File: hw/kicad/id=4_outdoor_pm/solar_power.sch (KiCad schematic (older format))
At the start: 5 parts

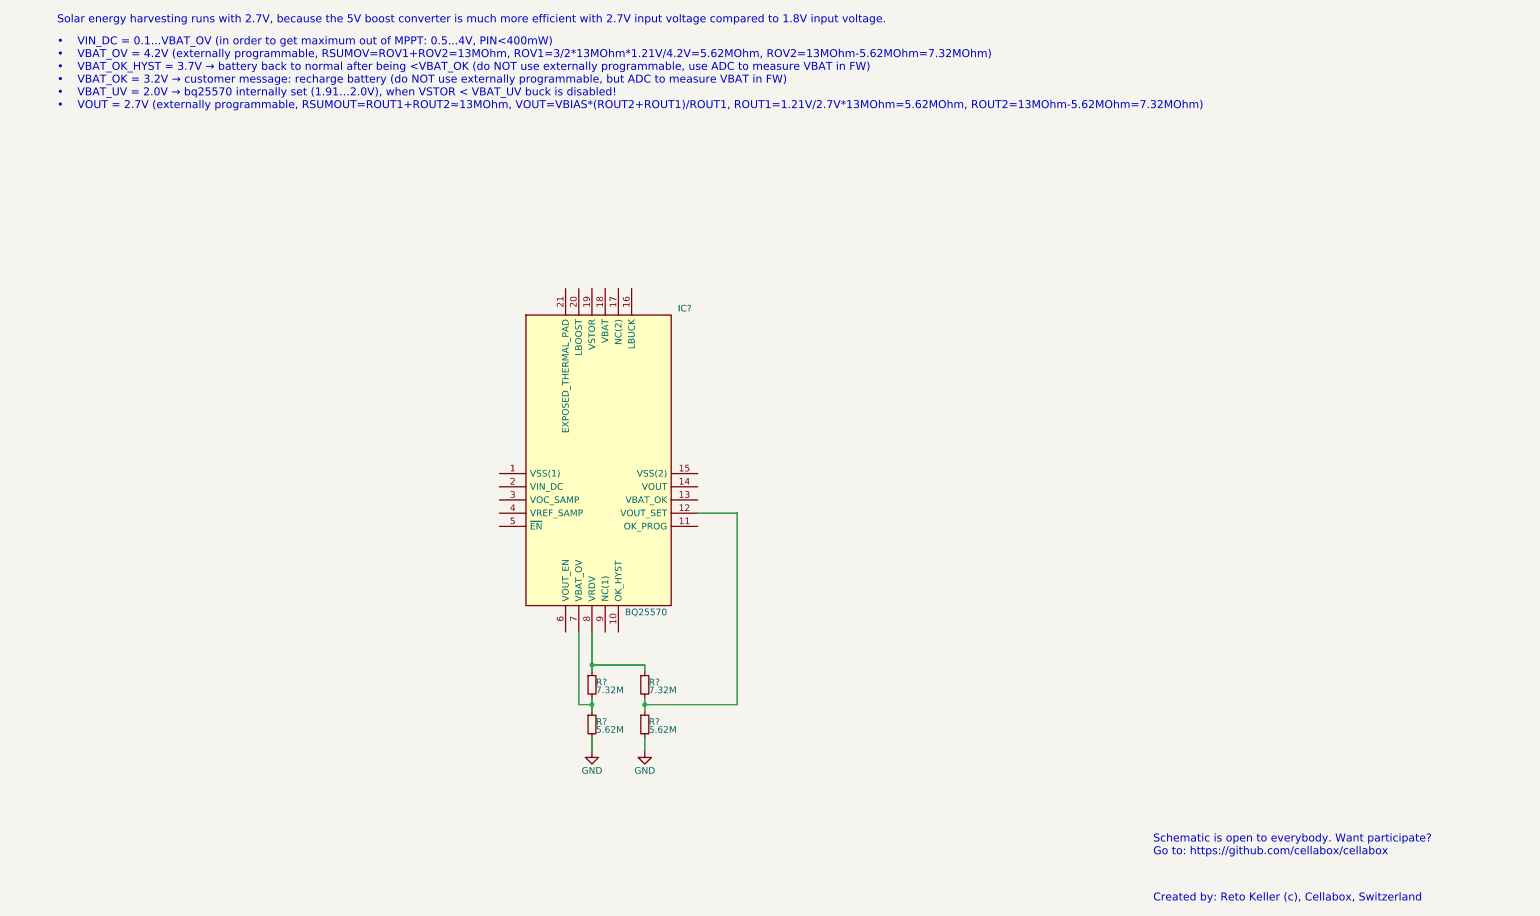
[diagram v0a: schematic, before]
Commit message: Datasheets added Schematic for outdoor PM extended
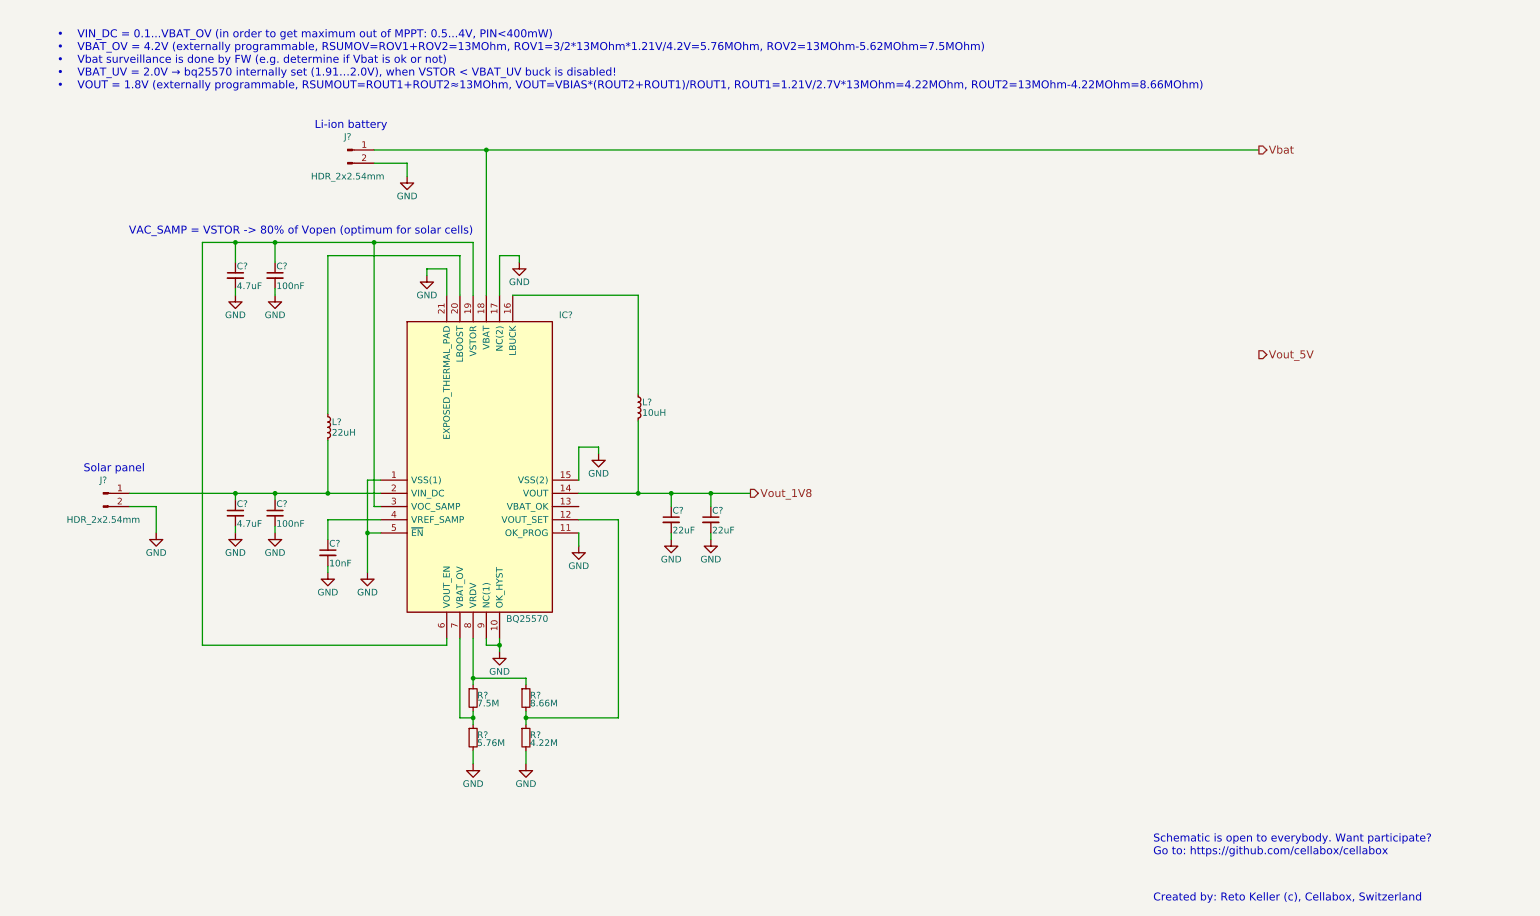
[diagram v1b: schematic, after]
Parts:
- added C? (x2): 22uF, symbol C_Small
- added C? (x2): 4.7uF, symbol C_Small
- added C? (x2): 100nF, symbol C_Small
- added C?: 10nF, symbol C_Small
- added J? (x2): HDR_2x2.54mm, symbol Conn_01x02_Male
- added L?: 10uH, symbol L_Small
- added L?: 22uH, symbol L_Small
- R?: value 7.32M -> 7.5M
- R?: value 5.62M -> 5.76M
- R?: value 5.62M -> 4.22M
- R?: value 7.32M -> 8.66M
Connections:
- net GND: now also IC?.1 (VSS(1)), IC?.10 (OK_HYST), IC?.11 (OK_PROG), IC?.15 (VSS(2)), IC?.17 (NC(2)), IC?.21 (EXPOSED_THERMAL_PAD), IC?.5 (~EN), IC?.9 (NC(1)), C?.2, C?.2, C?.2, C?.2, C?.2, C?.2, C?.2, J?.2 (Pin_2), J?.2 (Pin_2)
- net Vout_1V8: now reaches IC?.14 (VOUT)
- net Vout_1V8: now also C?.1, C?.1, L?.2
- net at IC?.16 (LBUCK): now also L?.1
- net Vbat: now reaches IC?.18 (VBAT)
- net Vbat: now also J?.1 (Pin_1)
- net at IC?.19 (VSTOR): now also IC?.3 (VOC_SAMP), IC?.6 (VOUT_EN), C?.1, C?.1
- net at IC?.2 (VIN_DC): now also C?.1, C?.1, J?.1 (Pin_1), L?.2
- net at IC?.20 (LBOOST): now also L?.1
- net at IC?.4 (VREF_SAMP): now also C?.1
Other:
- note added: "Li-ion battery"
- note added: "Solar panel"
- note added: "VAC_SAMP = VSTOR -> 80% of Vopen (optimum for solar cells)"
- note added: "• VIN_DC = 0.1...VBAT_OV (in order to get maximum out of MPPT: 0.5...4V, PIN<400mW)\n• VBAT_OV = 4.2V (externally programmable, RSUMOV=ROV1+ROV2=13MOhm, ROV1=3/2*13MOhm*1.21V/4.2V=5.76MOhm, ROV2=13MOhm-5.62MOhm=7.5MOhm)\n• Vbat surveillance is done by FW (e.g. determine if Vbat is ok or not)\n• VBAT_UV = 2.0V → bq25570 internally set (1.91…2.0V), when VSTOR < VBAT_UV buck is disabled!\n• VOUT = 1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"
- note removed: "Solar energy harvesting runs with 2.7V, because the 5V boost converter is much more efficient with 2.7V input voltage compared to 1.8V input voltage."
- note removed: "• VIN_DC = 0.1...VBAT_OV (in order to get maximum out of MPPT: 0.5...4V, PIN<400mW)\n• VBAT_OV = 4.2V (externally programmable, RSUMOV=ROV1+ROV2=13MOhm, ROV1=3/2*13MOhm*1.21V/4.2V=5.62MOhm, ROV2=13MOhm-5.62MOhm=7.32MOhm)\n• VBAT_OK_HYST = 3.7V → battery back to normal after being <VBAT_OK (do NOT use externally programmable, use ADC to measure VBAT in FW)\n• VBAT_OK = 3.2V → customer message: rec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"
- moved on the sheet: IC?, R?

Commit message: Updated schematics: battery surveillance.
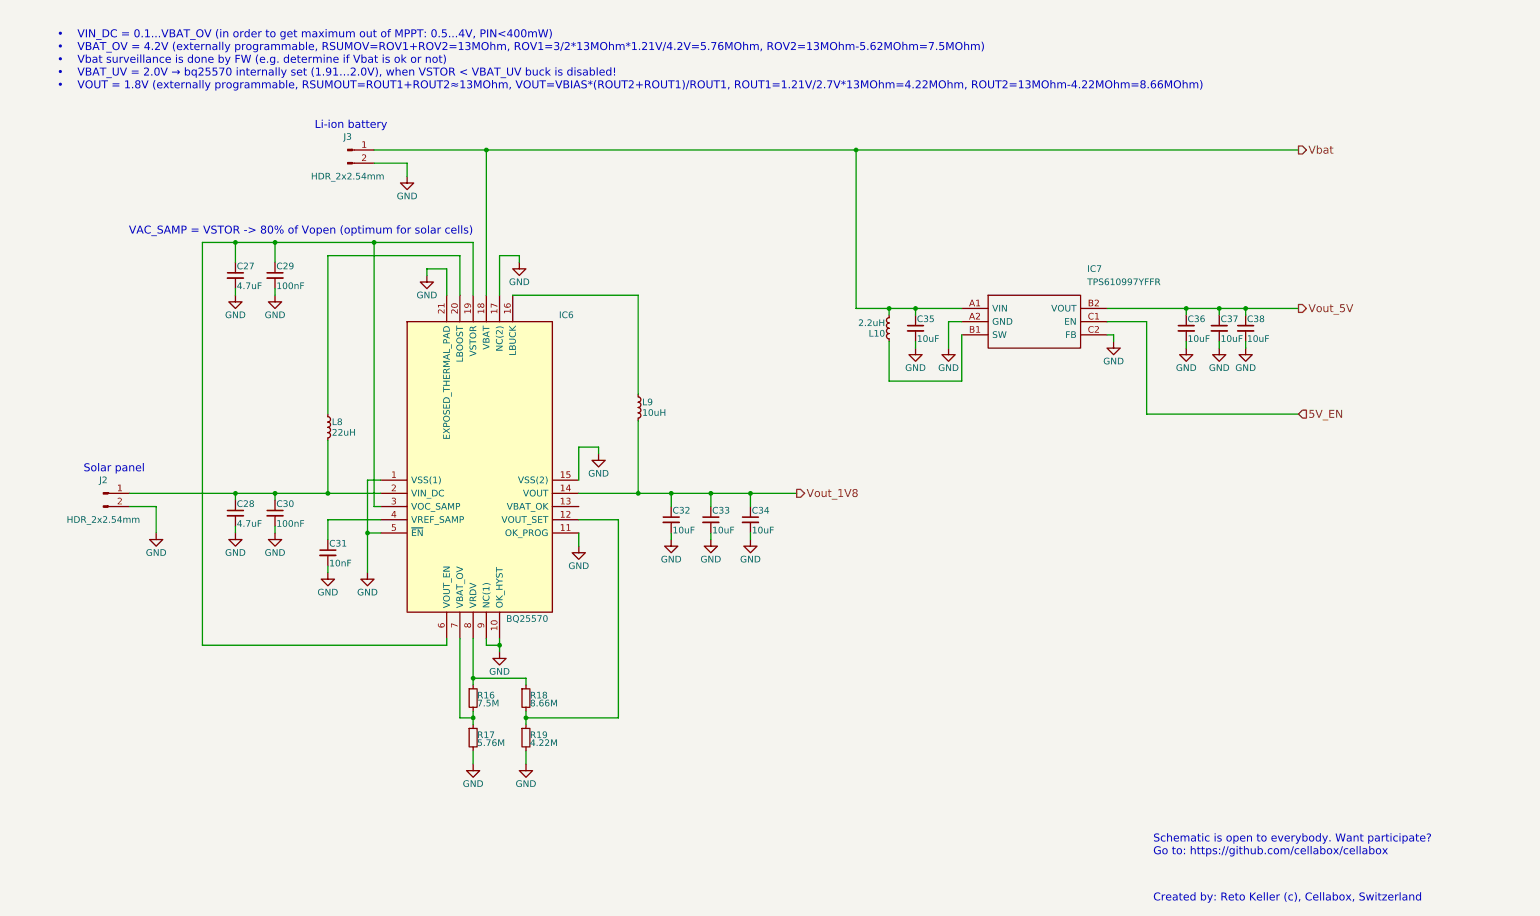
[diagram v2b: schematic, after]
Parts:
- removed C? (x2): 22uF, symbol C_Small
- added C32, C33, C34, C35, C36, C37, C38: 10uF, symbol C_Small
- added IC7: TPS610997YFFR, BGA6C40P2X3_88X123X62, symbol TPS610997YFFR
- added L10: 2.2uH, symbol L_Small
- gave numbers to parts that had none: 14
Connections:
- net GND: now also C32.2, C33.2, C34.2, C35.2, C36.2, C37.2, C38.2, IC7.A2 (GND), IC7.C2 (FB)
- net Vbat: now also C35.1, IC7.A1 (VIN), L10.2
- net Vout_1V8: now also C32.1, C33.1, C34.1
- net Vout_5V: now also C36.1, C37.1, C38.1, IC7.B2 (VOUT)
- new net: IC7.B1 (SW), L10.1
- new net 5V_EN: IC7.C1 (EN)
